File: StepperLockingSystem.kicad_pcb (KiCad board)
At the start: 4 copper layers, 54 x 84 mm, 106 parts, among them J1 Nerdstern, J10 MotorNTC, J11 Stepper, J12 HallEncoder, J2 DigitalLED, J3 Open+Close, J4 SWD, J5 6Pin DuPont 2.56mm, J6 5Pin DuPont 2.54mm, J7 LockState, J8 DoorState, J9 PowerConnector, Q1 IRLML0030, SW1 Reset, U1 STM32G0B1KET, U2 24LC64, U3 TC1185, U4 INA180A1, U5 USBLC6-2SC6, U6 USBLC6-2SC6, U7 TMC2209-LA, Y1 ABM3B-16MHz

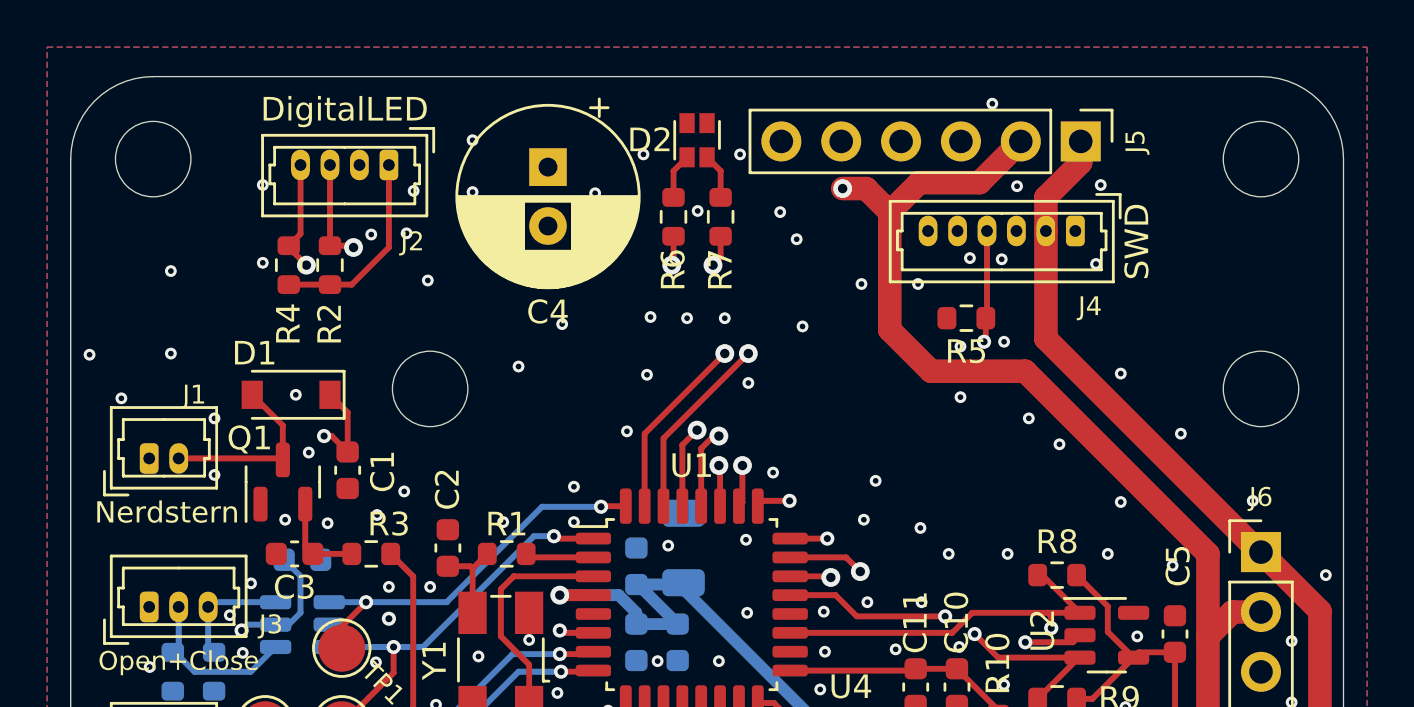
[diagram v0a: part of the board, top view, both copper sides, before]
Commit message: Change positions of mounting holes to middle
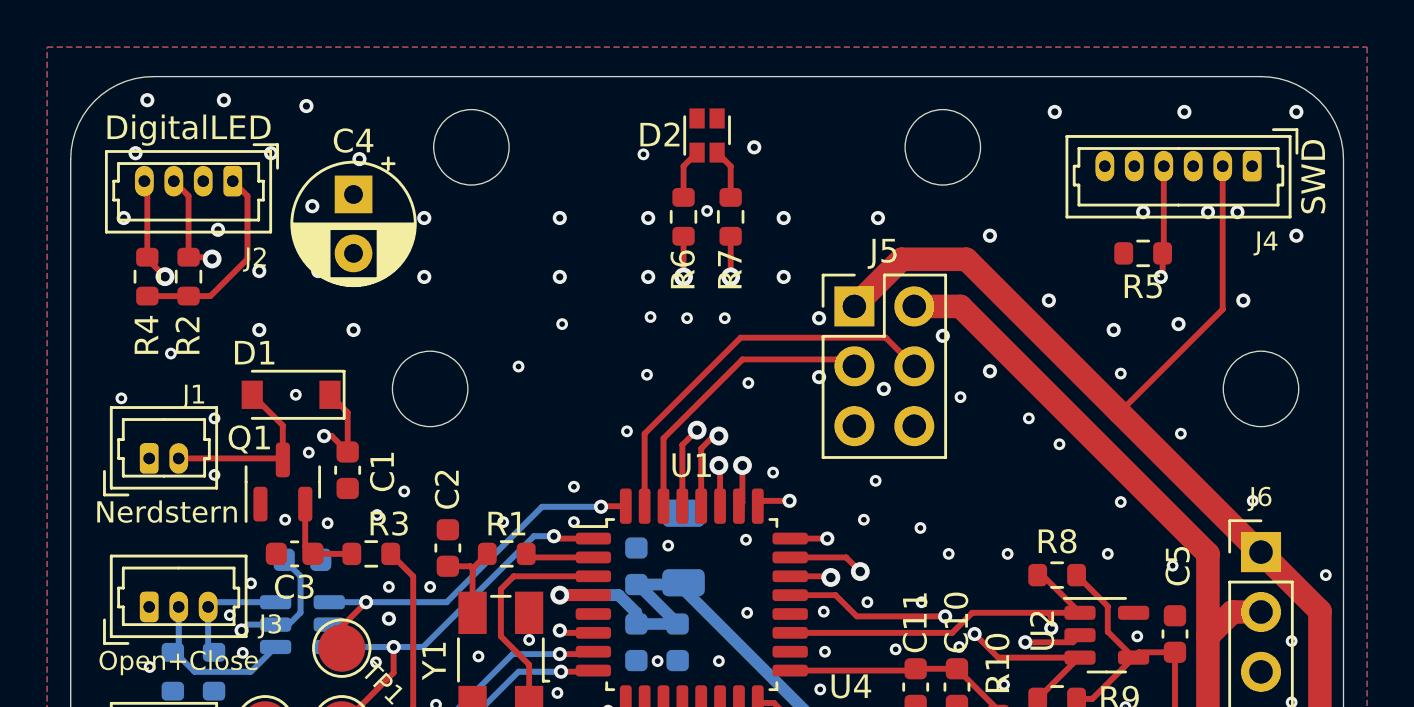
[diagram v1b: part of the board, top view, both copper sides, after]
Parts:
- C4: footprint Capacitor_THT:CP_Radial_D7.5mm_P2.50mm -> Capacitor_THT:CP_Radial_D5.0mm_P2.50mm
- J5: footprint Connector_PinHeader_2.54mm:PinHeader_1x06_P2.54mm_Vertical -> Connector_PinHeader_2.54mm:PinHeader_2x03_P2.54mm_Vertical
- moved H1 13.5 mm to (137.5, 66.8)
- moved H4 13.5 mm to (157.5, 66.8)
- moved J5 11.9 mm to (153.8, 73.6), turned to 0 degrees
- moved C4 8.33 mm to (132.5, 68.8)
- moved J4 7.99 mm to (170.6, 67.7)
- moved R5 7.99 mm to (166.0, 71.3)
- moved J2 6.66 mm to (127.4, 68.3)
- moved R2 6.02 mm to (125.5, 72.3)
- moved R4 6.02 mm to (123.8, 72.3)
- moved D2 0.47 mm to (147.5, 66.3)
- moved R6 0.43 mm to (146.5, 69.8)
- moved R7 0.43 mm to (148.5, 69.8)
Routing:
- net +3V3: track 209.7 -> 223.3 mm
- net /MCU/PINB6: track 20.7 -> 12.5 mm, vias 1 -> 0
- net /MCU/SWDIO: track 19.1 -> 26.5 mm
- net /MCU/SWCLK: track 18.7 -> 25.9 mm
- net /MCU/~{RST}: track 67.3 -> 73.8 mm
- net /ledData: track 25.7 -> 32.2 mm
- net /ledClock: track 27.5 -> 33.2 mm
- net /MCU/PINB7: track 20.0 -> 16.7 mm, vias 1 -> 0
- net +5V: track 172.6 -> 175.3 mm, vias 5 -> 4
- net GND: vias 241 -> 255

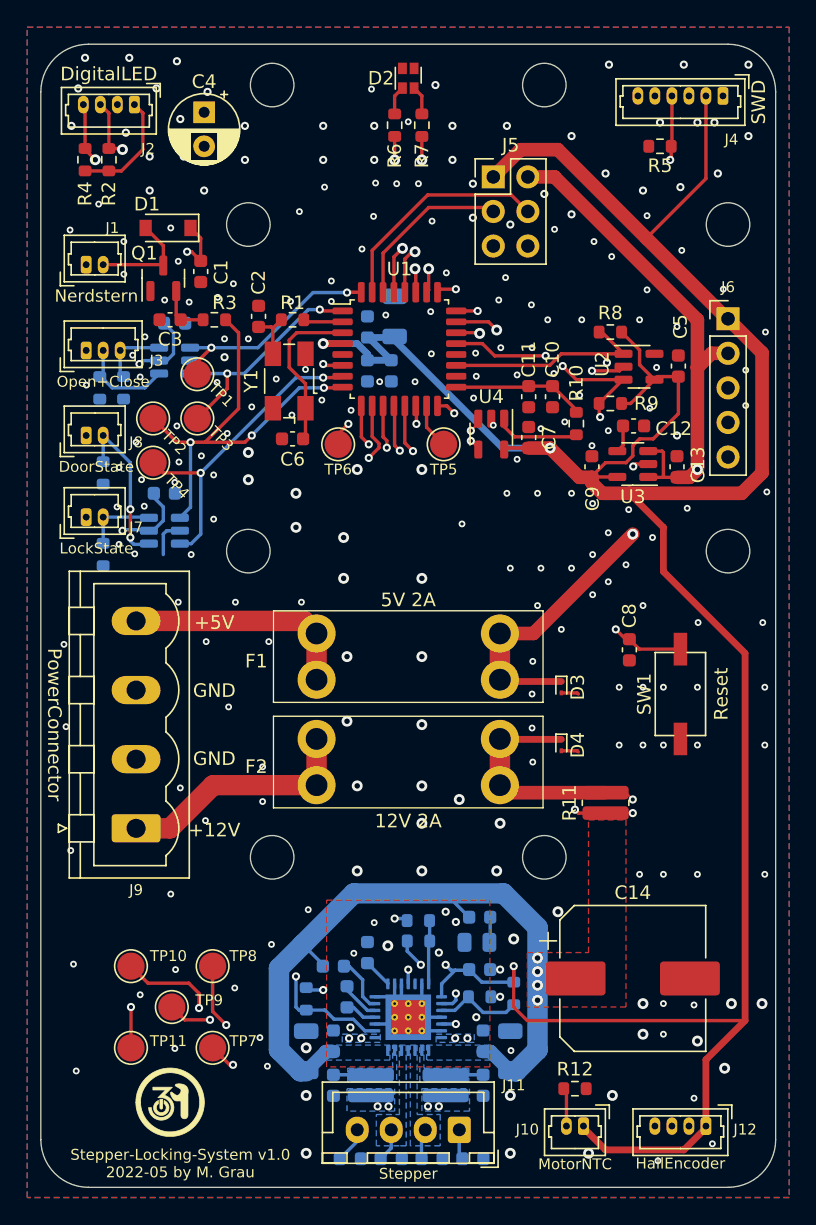
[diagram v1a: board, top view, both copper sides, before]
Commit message: Add holes for heat sink
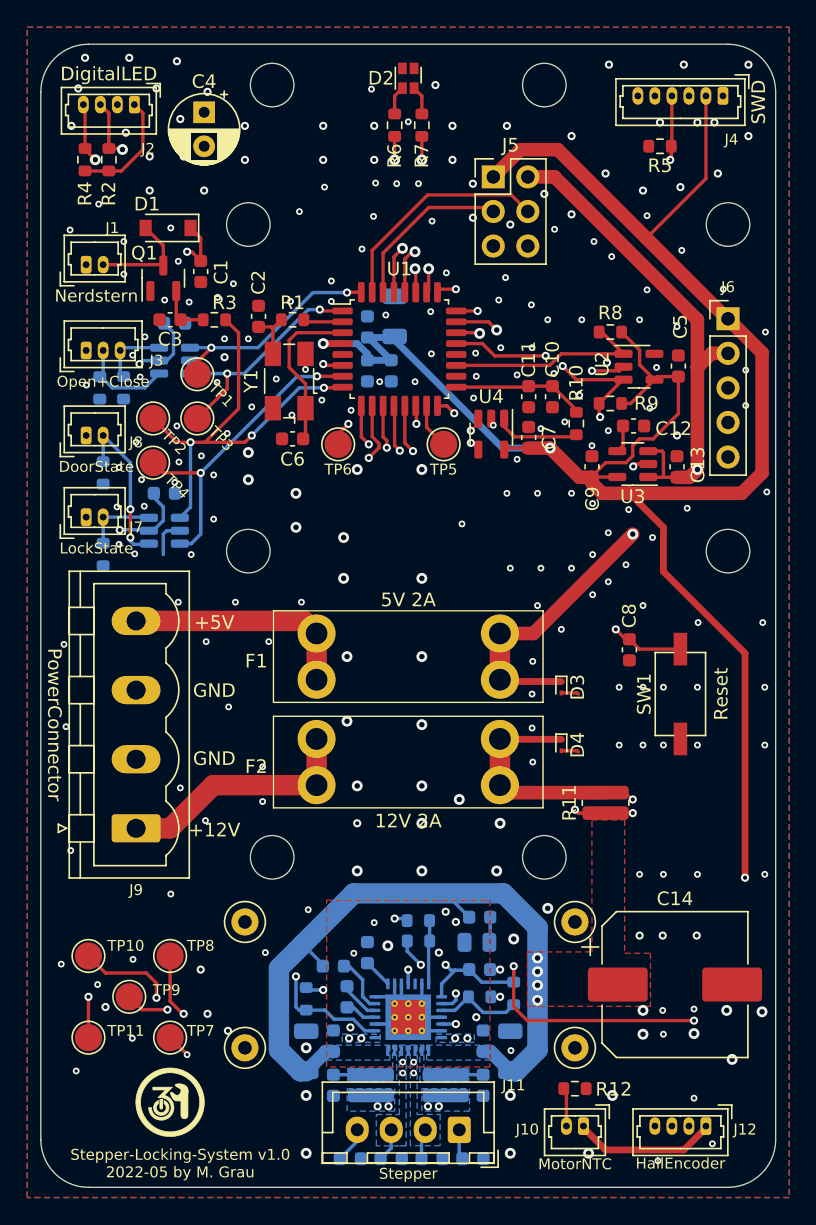
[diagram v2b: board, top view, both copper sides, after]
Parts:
- added REF**: TestPoint_Loop_D1.80mm_Drill1.0mm_Beaded, TestPoint:TestPoint_Loop_D1.80mm_Drill1.0mm_Beaded, F.Cu at (135.5, 128.3)
- added REF**: TestPoint_Loop_D1.80mm_Drill1.0mm_Beaded, TestPoint:TestPoint_Loop_D1.80mm_Drill1.0mm_Beaded, F.Cu at (159.8, 128.3)
- added REF**: TestPoint_Loop_D1.80mm_Drill1.0mm_Beaded, TestPoint:TestPoint_Loop_D1.80mm_Drill1.0mm_Beaded, F.Cu at (135.5, 137.6)
- added REF**: TestPoint_Loop_D1.80mm_Drill1.0mm_Beaded, TestPoint:TestPoint_Loop_D1.80mm_Drill1.0mm_Beaded, F.Cu at (159.8, 137.6)
- moved TP10 3.21 mm to (124.0, 130.8)
- moved TP11 3.21 mm to (124.0, 136.8)
- moved TP7 3.21 mm to (130.0, 136.8)
- moved TP8 3.21 mm to (130.0, 130.8)
- moved TP9 3.21 mm to (127.0, 133.8)
- moved C14 3.13 mm to (167.1, 132.9)
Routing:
- net /MCU/Stepper_Diag: track 64.1 -> 66.9 mm
- net /MCU/Stepper_Direction: track 71.4 -> 74.2 mm
- net /MCU/~{Stepper_Enable}: track 69.5 -> 72.3 mm
- net /MCU/Stepper_UART: track 63.1 -> 65.9 mm
- net /MCU/Stepper_Step: track 70.0 -> 72.8 mm
- net +3V3: vias 6 -> 8
- net GND: vias 255 -> 260
- net /StepperDriver/coilB_1: vias 0 -> 2
- net /StepperDriver/coilA_1: vias 0 -> 2
- added copper zone on In1.Cu, net /StepperDriver/coilA_1
- added copper zone on In1.Cu, net /StepperDriver/coilB_1

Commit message: Apply suggestions from tux: Single connector for signals Some (better) notes
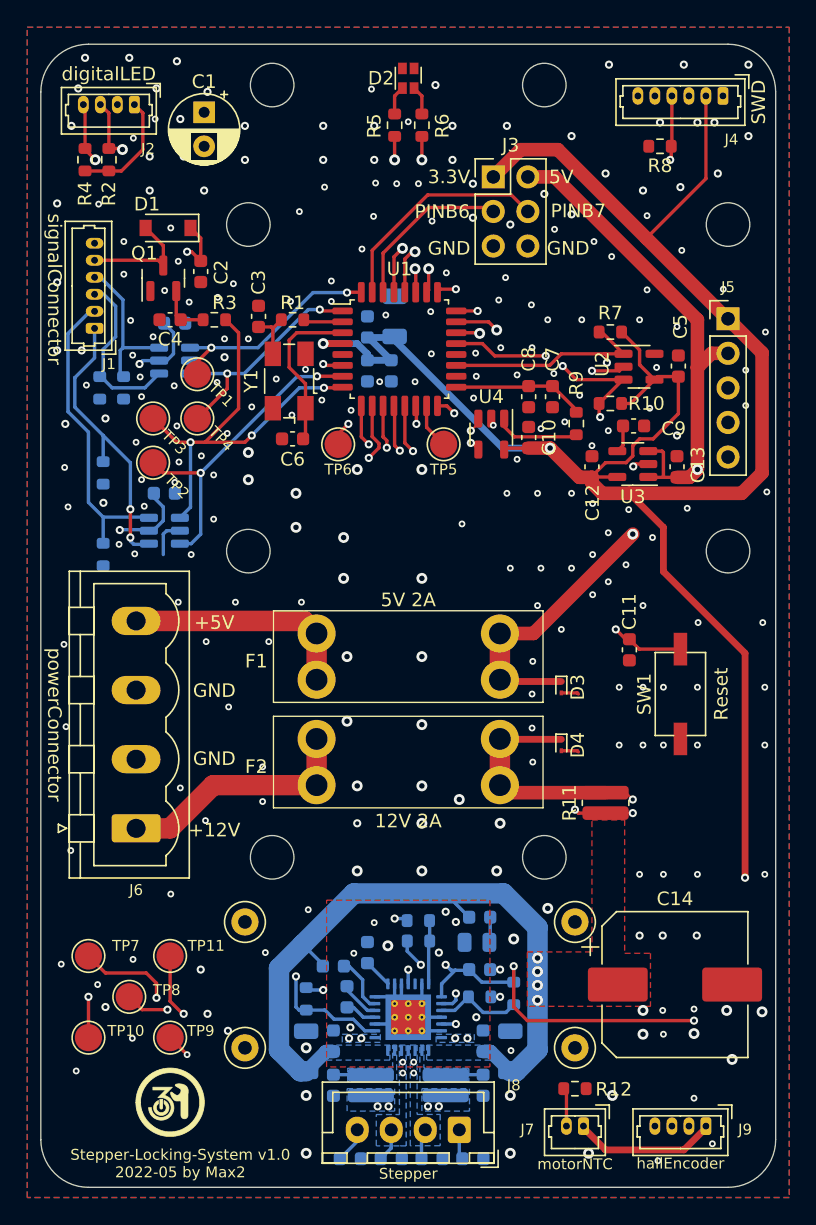
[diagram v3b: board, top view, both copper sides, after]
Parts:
- removed the J3 at (123.8, 86.3)
- removed the J7 at (123.8, 98.6)
- removed the J8 at (123.8, 92.6)
- J1: value Nerdstern -> signalConnector; footprint Connector_Molex:Molex_PicoBlade_53047-0210_1x02_P1.25mm_Vertical -> Connector_Molex:Molex_PicoBlade_53047-0610_1x06_P1.25mm_Vertical
- J2: value DigitalLED -> digitalLED
- J6: renamed from J9; value PowerConnector -> powerConnector
- J7: renamed from J10; value MotorNTC -> motorNTC
- J9: renamed from J12; value HallEncoder -> hallEncoder
- moved J1 4.72 mm to (124.5, 84.7), turned to 90 degrees
- renumbered C4 to C1, C7 to C10, C8 to C11, C9 to C12, C1 to C2, C2 to C3, C3 to C4, C10 to C7, C11 to C8, C12 to C9, H4 to H3, H3 to H4, J5 to J3, J6 to J5, J11 to J8, R9 to R10, R6 to R5, R7 to R6, R8 to R7, R5 to R8, R10 to R9, TP11 to TP10, TP8 to TP11, TP4 to TP2, TP2 to TP3, TP3 to TP4, TP10 to TP7, TP9 to TP8, TP7 to TP9
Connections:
- D1 pad 2: Net-(D1-Pad2) -> /MCU/NerdsternRelayGround
- J1 pad 1: VCC -> /MCU/DoorStateRaw
- J1 pad 2: Net-(D1-Pad2) -> /MCU/LockStateRaw
- Q1 pad 3: Net-(D1-Pad2) -> /MCU/NerdsternRelayGround
- R13 pad 1: Net-(J3-Pad3) -> /MCU/OpenButtonRaw
- R14 pad 1: Net-(J7-Pad2) -> /MCU/LockStateRaw
- R15 pad 1: Net-(J8-Pad2) -> /MCU/DoorStateRaw
- R16 pad 1: Net-(J3-Pad2) -> /MCU/CloseButtonRaw
- U5 pad 4: Net-(J3-Pad2) -> /MCU/CloseButtonRaw
- U5 pad 6: Net-(J3-Pad3) -> /MCU/OpenButtonRaw
- U6 pad 4: Net-(J8-Pad2) -> /MCU/DoorStateRaw
- U6 pad 6: Net-(J7-Pad2) -> /MCU/LockStateRaw
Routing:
- net +5V: track 175.3 -> 152.7 mm
- net /MCU/LockStateRaw: track 0.00 -> 22.5 mm
- net /MCU/DoorStateRaw: track 0.00 -> 21.3 mm, vias 0 -> 2
- net /MCU/CloseButtonRaw: track 0.00 -> 12.7 mm
- net Net-(J8-Pad2): track 12.0 -> 0.00 mm, vias 2 -> 0
- net /MCU/OpenButtonRaw: track 0.00 -> 11.3 mm
- net /MCU/NerdsternRelayGround: track 0.00 -> 8.51 mm
- net VCC: track 161.9 -> 153.9 mm
- net Net-(D1-Pad2): track 7.75 -> 0.00 mm
- net Net-(J3-Pad2): track 7.17 -> 0.00 mm
- net Net-(J7-Pad2): track 5.31 -> 0.00 mm
- net Net-(J3-Pad3): track 4.97 -> 0.00 mm
- net GND: vias 260 -> 270
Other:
- board text added: "Stepper-Locking-System v1.0 2022-05 by Max2"
- board text removed: "Stepper-Locking-System v1.0 2022-05 by M. Grau"

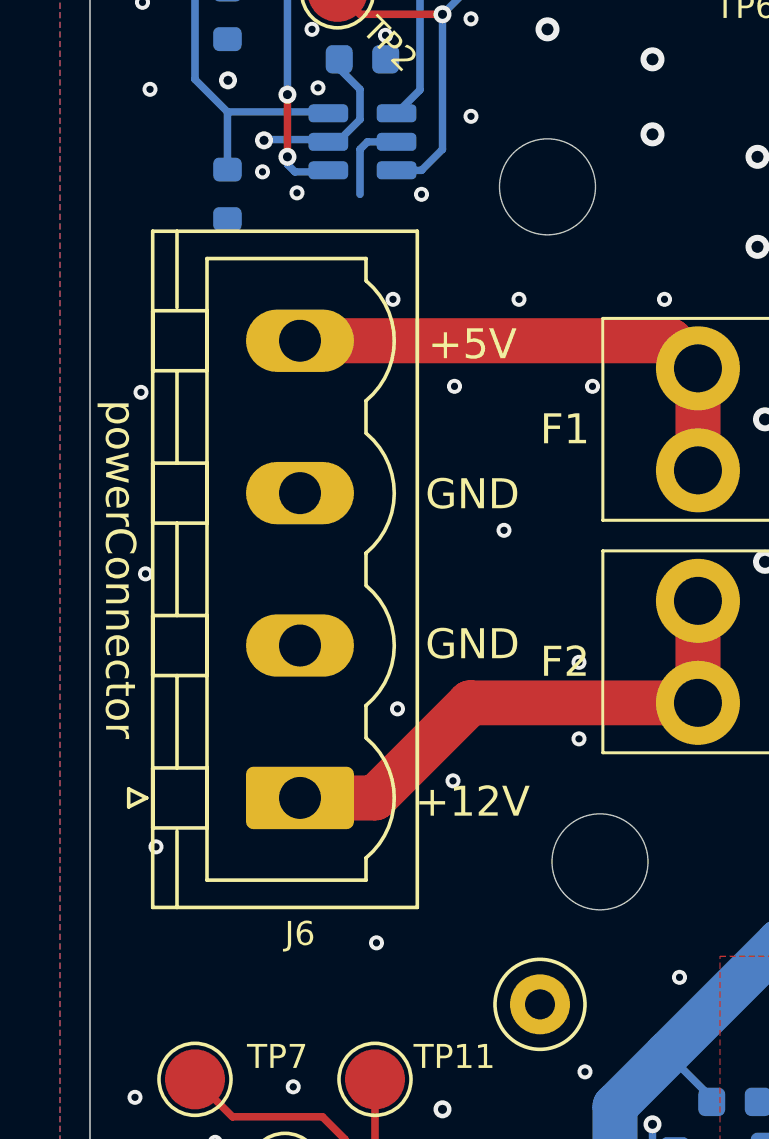
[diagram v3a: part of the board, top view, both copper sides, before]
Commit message: Change power input pin out Update exported stuffs Update ReadMe
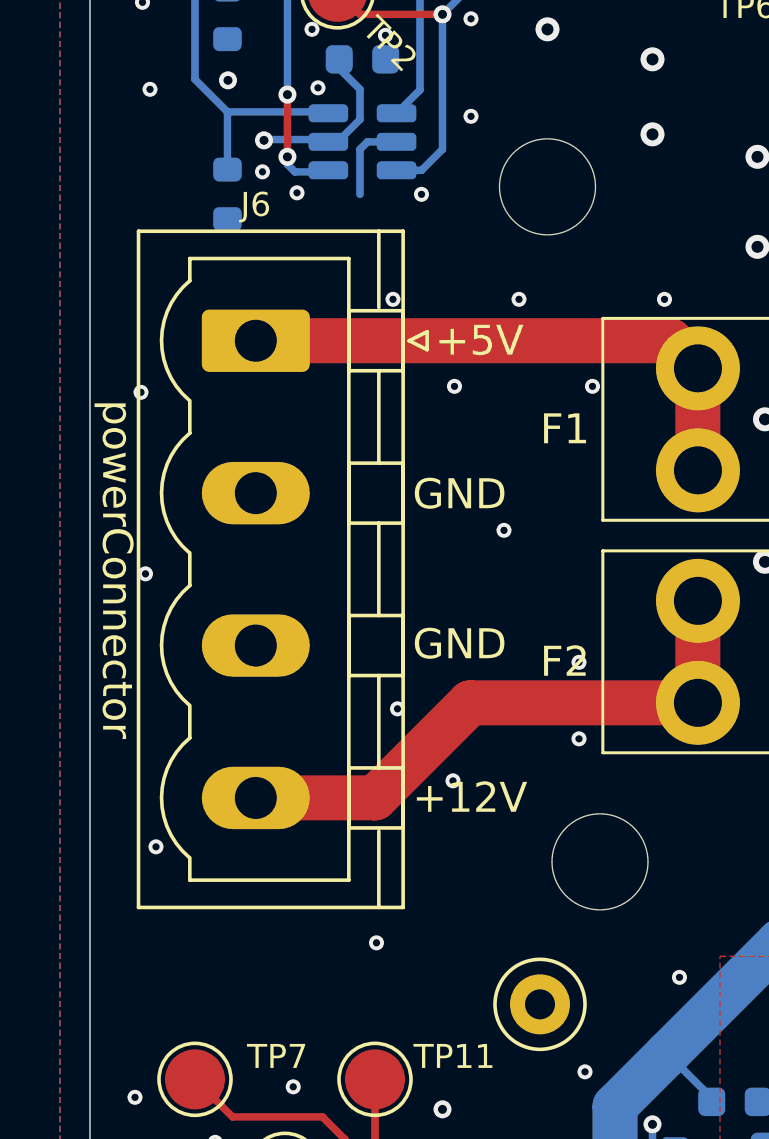
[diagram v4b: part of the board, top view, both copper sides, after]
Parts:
- moved J6 15.3 mm to (126.0, 106.2), turned to -90 degrees
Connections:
- J6 pad 1: Net-(F2-Pad1) -> Net-(F1-Pad1)
- J6 pad 4: Net-(F1-Pad1) -> Net-(F2-Pad1)
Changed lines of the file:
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@@
   )
   (footprint "Connector_Phoenix_MSTB:PhoenixContact_MSTBVA_2,5_4-G-5,08_1x04_P5.08mm_Vertical" (layer "F.Cu")
-    (at 127.5 121.47 90)
+    (at 126.0275 106.23 -90)
     (descr "Generic Phoenix Contact connector footprint for: MSTBVA_2,5/4-G-5,08; number of pins: 04; pin pitch: 5.08mm; Vertical || order number: 1755752 12A || order number: 1924321 16A (HC)")
     (tags "phoenix_contact connector MSTBVA_01x04_G_5.08mm")
@@
     (property "Sheetname" "")
     (attr through_hole)
-    (fp_text reference "J6" (at -4.53 0 180) (layer "F.SilkS")
+    (fp_text reference "J6" (at -4.53 0) (layer "F.SilkS")
       (effects (font (size 0.8 0.8) (thickness 0.15)))
     )
-    (fp_text value "powerConnector" (at 7.62 -6 270 unlocked) (layer "F.SilkS")
+    (fp_text value "powerConnector" (at 7.62 4.6275 -90 unlocked) (layer "F.SilkS")
       (effects (font (size 1 1) (thickness 0.15)))
     )
-    (fp_text user "GND" (at 10.12 5.75 unlocked) (layer "F.SilkS")
-      (effects (font (size 1 1) (thickness 0.15)))
+    (fp_text user "GND" (at 10.12 -5.2225 unlocked) (layer "F.SilkS")
+      (effects (font (size 1 1) (thickness 0.15)) (justify left))
     )
-    (fp_text user "GND" (at 5.12 5.75 unlocked) (layer "F.SilkS")
-      (effects (font (size 1 1) (thickness 0.15)))
+    (fp_text user "GND" (at 5.12 -5.2225 unlocked) (layer "F.SilkS")
+      (effects (font (size 1 1) (thickness 0.15)) (justify left))
     )
-    (fp_text user "+5V" (at 15.12 5.75 unlocked) (layer "F.SilkS")
-      (effects (font (size 1 1) (thickness 0.15)))
+    (fp_text user "+5V" (at 0 -5.9725 unlocked) (layer "F.SilkS")
+      (effects (font (size 1 1) (thickness 0.15)) (justify left))
     )
-    (fp_text user "+12V" (at -0.13 5.75 unlocked) (layer "F.SilkS")
-      (effects (font (size 1 1) (thickness 0.15)))
+    (fp_text user "+12V" (at 15.24 -5.2225 unlocked) (layer "F.SilkS")
+      (effects (font (size 1 1) (thickness 0.15)) (justify left))
     )
     (fp_text user "${REFERENCE}" (at 7.62 -4.1 90) (layer "F.Fab")
@@
     (fp_line (start 0 -2.55) (end -0.5 -3.55) (layer "F.Fab") (width 0.1))
     (fp_line (start 18.78 -4.8) (end -3.54 -4.8) (layer "F.Fab") (width 0.1))
-    (pad "1" thru_hole roundrect (at 0 0 90) (size 2.08 3.6) (drill 1.4) (layers *.Cu *.Mask) (roundrect_rratio 0.120192)
-      (net 40 "Net-(F2-Pad1)") (pinfunction "Pin_1") (pintype "passive"))
-    (pad "2" thru_hole oval (at 5.08 0 90) (size 2.08 3.6) (drill 1.4) (layers *.Cu *.Mask)
+    (pad "1" thru_hole roundrect (at 0 0 270) (size 2.08 3.6) (drill 1.4) (layers *.Cu *.Mask) (roundrect_rratio 0.120192)
+      (net 39 "Net-(F1-Pad1)") (pinfunction "Pin_1") (pintype "passive"))
+    (pad "2" thru_hole oval (at 5.08 0 270) (size 2.08 3.6) (drill 1.4) (layers *.Cu *.Mask)
       (net 1 "GND") (pinfunction "Pin_2") (pintype "passive"))
-    (pad "3" thru_hole oval (at 10.16 0 90) (size 2.08 3.6) (drill 1.4) (layers *.Cu *.Mask)
+    (pad "3" thru_hole oval (at 10.16 0 270) (size 2.08 3.6) (drill 1.4) (layers *.Cu *.Mask)
       (net 1 "GND") (pinfunction "Pin_3") (pintype "passive"))
-    (pad "4" thru_hole oval (at 15.24 0 90) (size 2.08 3.6) (drill 1.4) (layers *.Cu *.Mask)
-      (net 39 "Net-(F1-Pad1)") (pinfunction "Pin_4") (pintype "passive"))
+    (pad "4" thru_hole oval (at 15.24 0 270) (size 2.08 3.6) (drill 1.4) (layers *.Cu *.Mask)
+      (net 40 "Net-(F2-Pad1)") (pinfunction "Pin_4") (pintype "passive"))
     (model "${KICAD6_3DMODEL_DIR}/Connector_Phoenix_MSTB.3dshapes/PhoenixContact_MSTBVA_2,5_4-G-5,08_1x04_P5.08mm_Vertical.wrl"
       (offset (xyz 0 0 0))
